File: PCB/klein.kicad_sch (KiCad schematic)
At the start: 80 parts, among them J1 Conn_01x12, J2 Haptic Buzz, J3 Conn_01x04, J5 OLED-128x64, SW1 MX_SW_HS, SW10 MX_SW_HS, SW11 MX_SW_HS, SW12 MX_SW_HS, SW13 MX_SW_HS, SW14 MX_SW_HS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

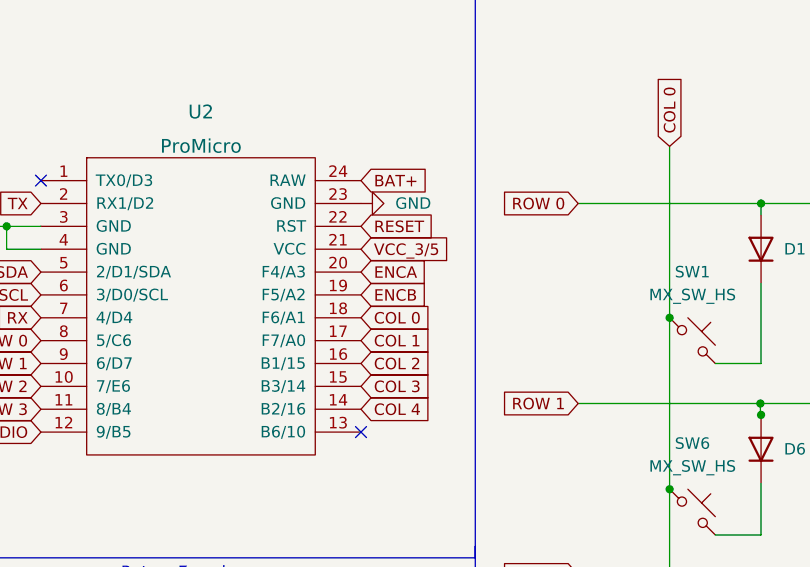
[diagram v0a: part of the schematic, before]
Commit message: Fix PCB Encoder Routes (Typo in Schematic) and IBOM project name fix
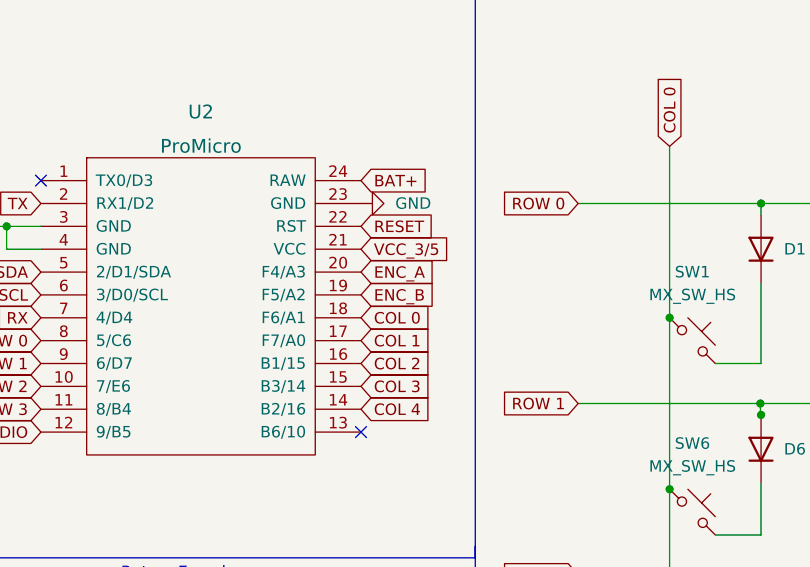
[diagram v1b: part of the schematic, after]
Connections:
- net ENCA is gone; now on net ENC_A: U2.20 (F4/A3)
- net ENCB is gone; now on net ENC_B: U2.19 (F5/A2)
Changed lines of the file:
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@@
     )
   )
-  (global_label "ENCA" (shape input) (at 135.89 44.45 0) (fields_autoplaced)
+  (global_label "ENC_A" (shape input) (at 135.89 44.45 0) (fields_autoplaced)
     (effects (font (size 1.27 1.27)) (justify left))
-    (property "Intersheet References" "${INTERSHEET_REFS}" (id 0) (at 143.1412 44.3706 0)
+    (property "Intersheet References" "${INTERSHEET_REFS}" (id 0) (at 144.1088 44.3706 0)
       (effects (font (size 1.27 1.27)) (justify left) hide)
     )
@@
     )
   )
-  (global_label "ENCB" (shape input) (at 135.89 46.99 0) (fields_autoplaced)
+  (global_label "ENC_B" (shape input) (at 135.89 46.99 0) (fields_autoplaced)
     (effects (font (size 1.27 1.27)) (justify left))
-    (property "Intersheet References" "${INTERSHEET_REFS}" (id 0) (at 143.3226 46.9106 0)
+    (property "Intersheet References" "${INTERSHEET_REFS}" (id 0) (at 144.2902 46.9106 0)
       (effects (font (size 1.27 1.27)) (justify left) hide)
     )

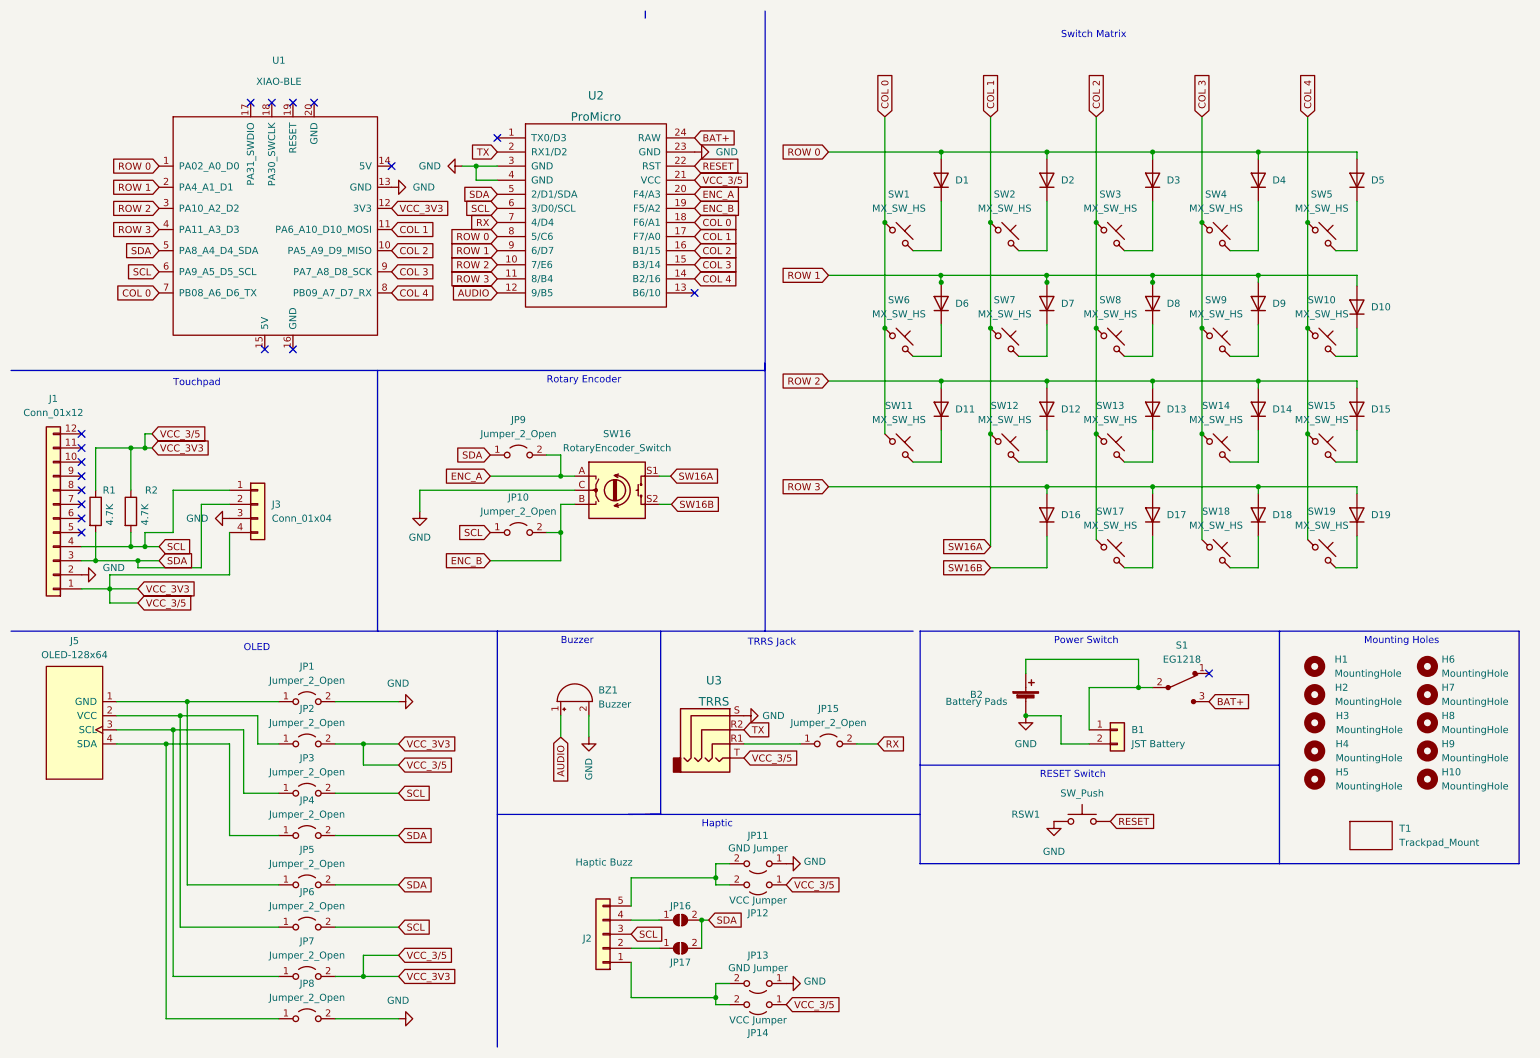
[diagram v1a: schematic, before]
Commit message: Removed TRRS jumper
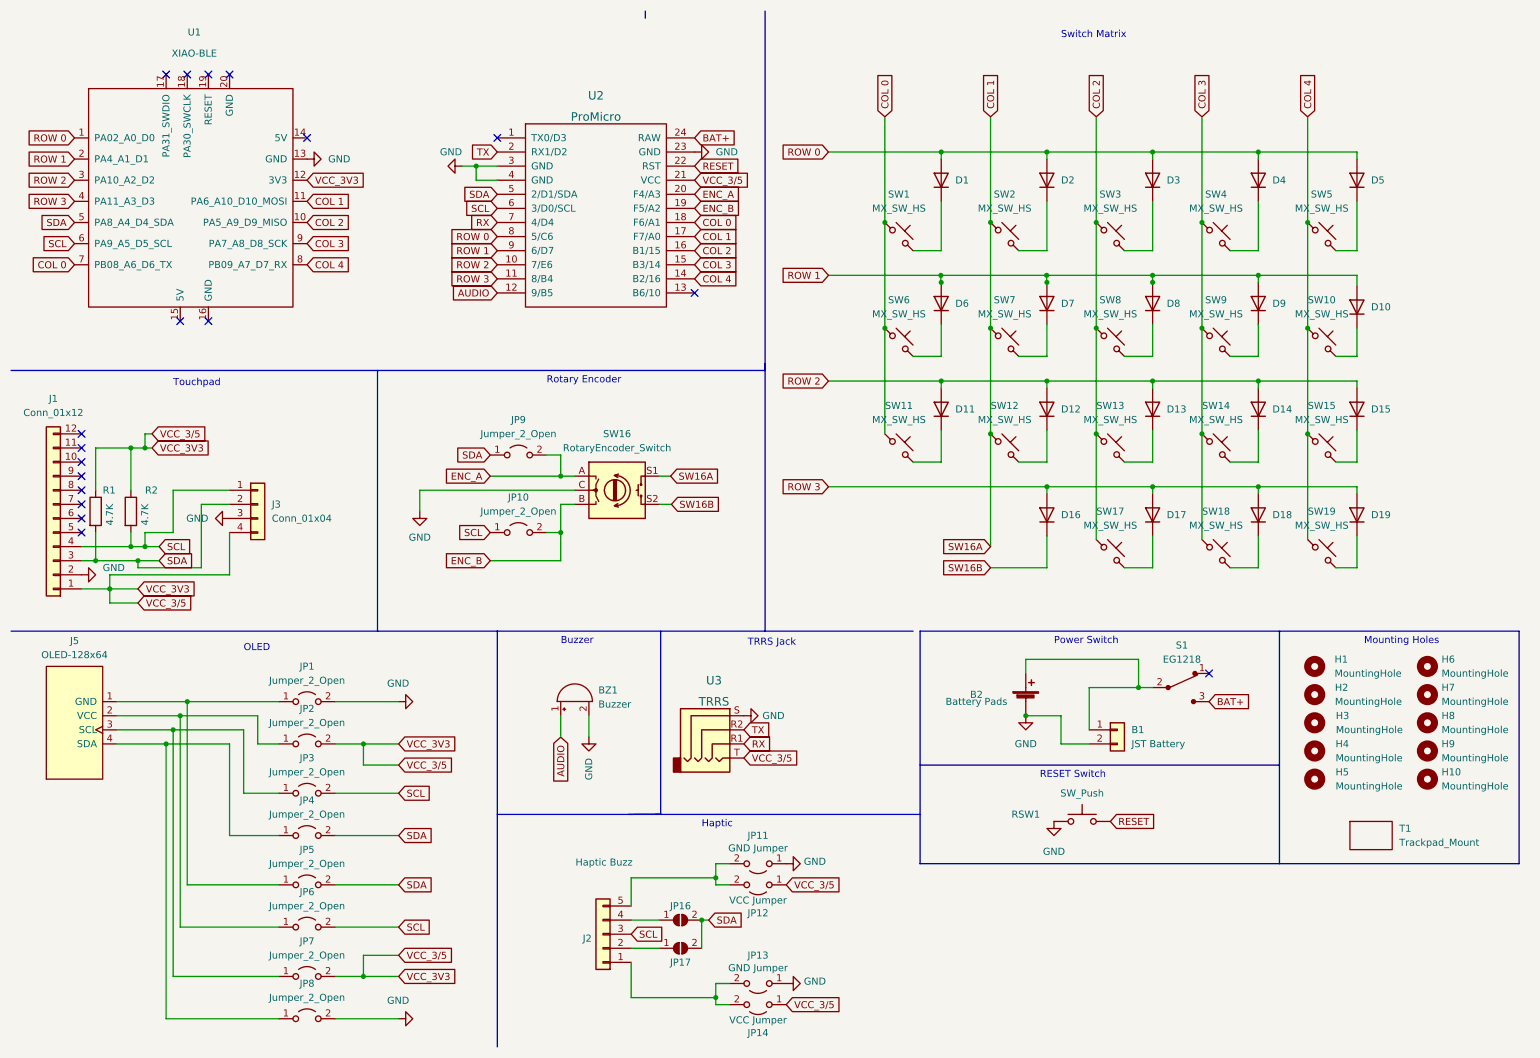
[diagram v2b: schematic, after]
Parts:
- removed JP15: Jumper_2_Open, Jumper:SolderJumper-2_P1.3mm_Open_RoundedPad1.0x1.5mm, symbol Jumper:Jumper_2_Open
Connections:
- net RX: now also U3.R1
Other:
- moved on the sheet: U1
